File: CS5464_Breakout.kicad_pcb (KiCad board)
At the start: 2 copper layers, 35.6 x 27.9 mm, 25 parts, among them J1 Conn_01x10, U1 CS5464-ISZ, Y1 Crystal

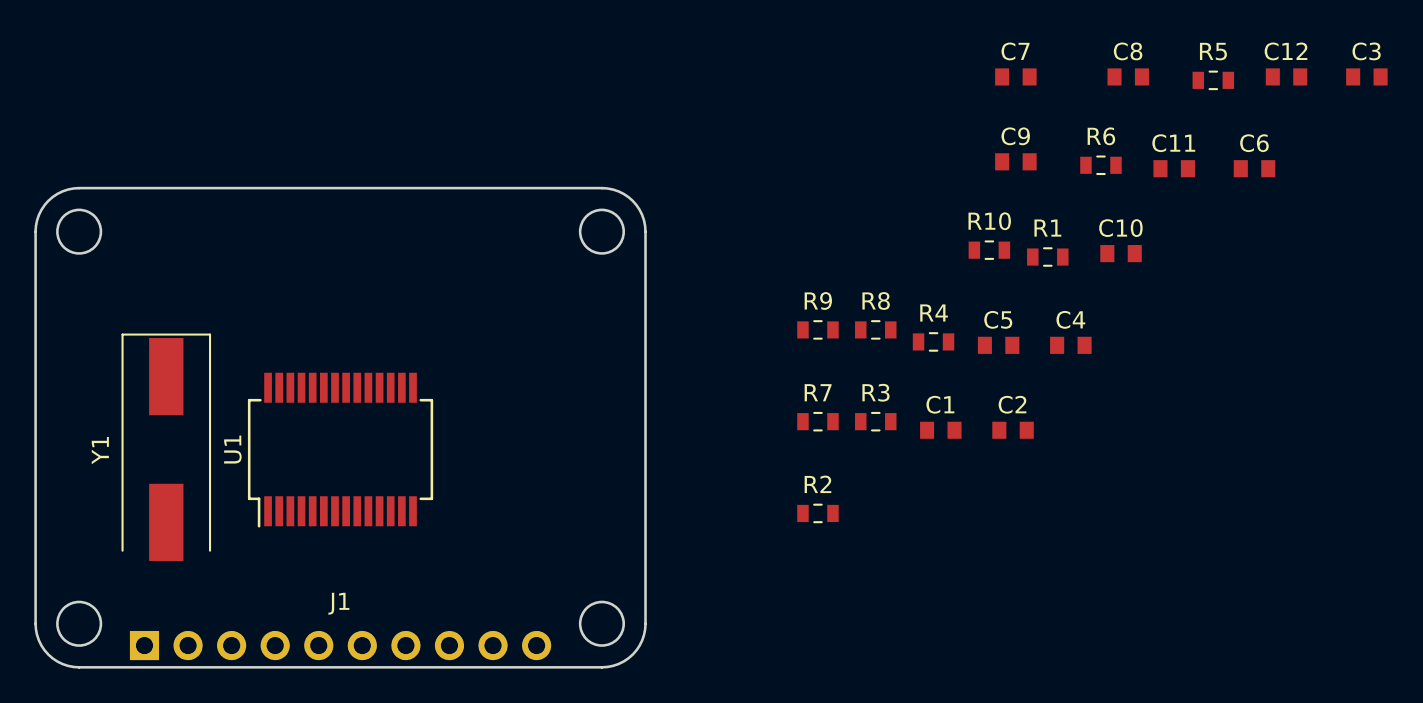
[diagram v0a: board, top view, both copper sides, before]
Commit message: Add logos and part placement
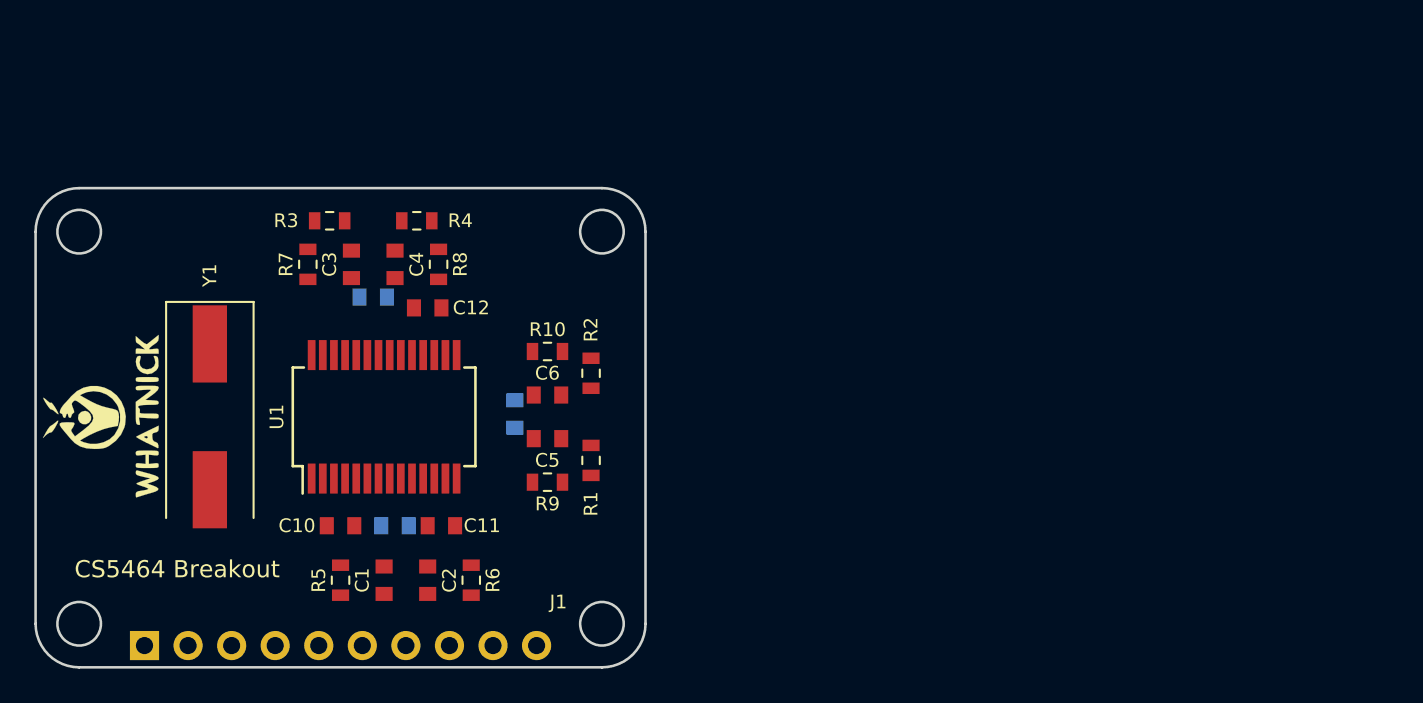
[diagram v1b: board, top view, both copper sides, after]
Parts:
- added G1: LOGO, Whatnick_logo:Whatnick_logo, F.Cu at (114.3, 93.3)
- added LOGO1: Logo_Open_Hardware_Small, Symbol:OSHW-Logo2_7.3x6mm_SilkScreen, B.Cu at (128.9, 94.0)
- C7, C8, C9: moved to B.Cu
- R1, R2, R3, R4: value 1K -> 2.4R
- moved C3 60.2 mm to (128.9, 84.5), turned to 90 degrees
- moved R5 58.6 mm to (128.3, 102.9), turned to 270 degrees
- moved C12 51.9 mm to (133.3, 87.0)
- moved C10 48.2 mm to (128.3, 99.7)
- moved C11 47.5 mm to (134.2, 99.7), turned to 180 degrees
- moved C8 45.9 mm to (130.2, 86.4)
- moved C7 44.7 mm to (131.4, 99.7)
- moved R6 44.0 mm to (135.9, 102.9), turned to 270 degrees
- moved C6 43.3 mm to (140.3, 92.1), turned to 180 degrees
- moved C4 39.7 mm to (131.4, 84.5), turned to 270 degrees
- moved C2 35.2 mm to (133.3, 102.9), turned to 90 degrees
- moved R3 33.9 mm to (127.6, 81.9), turned to 180 degrees
- moved C1 33.6 mm to (130.8, 102.9), turned to 270 degrees
- moved C9 32.7 mm to (138.4, 93.2), turned to 90 degrees
- moved R7 31.1 mm to (126.4, 84.5), turned to 90 degrees
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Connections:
- net Net-(U1-Pad23) renamed ~RESET
- net Net-(U1-Pad27) renamed MOSI
- net Net-(U1-Pad5) renamed SCLK
- net Net-(U1-Pad6) renamed MISO
- net Net-(U1-Pad7) renamed ~CS
- C10 pad 2: Net-(C10-Pad2) -> GND
- C11 pad 1: Net-(C11-Pad1) -> GND
- C11 pad 2: Net-(C11-Pad2) -> VREF
- C12 pad 1: Net-(C12-Pad1) -> Net-(C10-Pad1)
- C12 pad 2: Net-(C12-Pad2) -> GND
- C3 pad 1: IIN+ -> IIN1+
- C4 pad 2: IIN- -> IIN1-
- C8 pad 1: IIN+ -> IIN1+
- C8 pad 2: IIN- -> IIN1-
- R7 pad 1: IIN+ -> IIN1+
- R8 pad 1: IIN- -> IIN1-
- U1 pad 10: Net-(U1-Pad10) -> VIN-
- U1 pad 11: Net-(U1-Pad11) -> VREF
- U1 pad 12: Net-(U1-Pad12) -> VREF
- U1 pad 15: Net-(U1-Pad15) -> IIN2-
- U1 pad 16: Net-(U1-Pad16) -> IIN2+
- U1 pad 18: Net-(U1-Pad18) -> Net-(C10-Pad1)
- U1 pad 19: Net-(U1-Pad19) -> IIN1-
- U1 pad 20: Net-(U1-Pad20) -> IIN1+
- U1 pad 3: Net-(U1-Pad3) -> Net-(C10-Pad1)
- U1 pad 9: Net-(U1-Pad9) -> VIN+
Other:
- board text added: "CS5464 Breakout"

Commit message: Update schematic and PCB
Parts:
- added CPUCLK1: CPUCLK, TestPoint:TestPoint_Pad_1.5x1.5mm, B.Cu at (119.4, 96.5)
- added MODE1: MODE, TestPoint:TestPoint_Pad_1.5x1.5mm, B.Cu at (122.6, 96.5)
- added PFMON1: PFMON, TestPoint:TestPoint_Pad_1.5x1.5mm, B.Cu at (122.6, 90.2)
- added ~E1: ~E1, TestPoint:TestPoint_Pad_1.5x1.5mm, B.Cu at (116.2, 96.5)
- added ~E2: ~E2, TestPoint:TestPoint_Pad_1.5x1.5mm, B.Cu at (113.0, 96.5)
- added ~E3: ~E3, TestPoint:TestPoint_Pad_1.5x1.5mm, B.Cu at (119.4, 90.2)
- added ~INT1: ~INT, TestPoint:TestPoint_Pad_1.5x1.5mm, B.Cu at (113.0, 90.2)
- added ~RESET1: ~RESET, TestPoint:TestPoint_Pad_1.5x1.5mm, B.Cu at (116.2, 90.2)
- moved LOGO1 5.75 mm to (134.6, 93.3), turned to 270 degrees
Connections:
- net Net-(J1-Pad5) renamed CS
- C10 pad 1: Net-(C10-Pad1) -> +3V3
- C12 pad 1: Net-(C10-Pad1) -> +3V3
- J1 pad 1: Net-(J1-Pad1) -> +3V3
- J1 pad 10: Net-(J1-Pad10) -> GND
- J1 pad 2: Net-(J1-Pad2) -> VP
- J1 pad 3: Net-(J1-Pad3) -> VN
- J1 pad 4: Net-(J1-Pad4) -> SCLK
- J1 pad 6: Net-(J1-Pad6) -> MISO
- J1 pad 7: Net-(J1-Pad7) -> MOSI
- J1 pad 8: Net-(J1-Pad8) -> IP
- J1 pad 9: Net-(J1-Pad9) -> IN
- U1 pad 18: Net-(C10-Pad1) -> +3V3
- U1 pad 23: ~RESET -> Net-(U1-Pad23)
- U1 pad 3: Net-(C10-Pad1) -> +3V3

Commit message: Complete place and route and generate Gerbers
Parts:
- added IN2: IN2, TestPoint:TestPoint_Pad_1.5x1.5mm, B.Cu at (143.4, 91.5)
- added IP2: IP2, TestPoint:TestPoint_Pad_1.5x1.5mm, B.Cu at (143.4, 94.5)
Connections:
- J1 pad 5: CS -> ~CS
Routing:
- net GND: track 0.00 -> 70.4 mm, vias 0 -> 13
- net IP: track 0.00 -> 29.8 mm, vias 0 -> 1
- net +3V3: track 0.00 -> 29.7 mm
- net IN: track 0.00 -> 26.9 mm, vias 0 -> 1
- net Net-(U1-Pad26): track 0.00 -> 19.8 mm, vias 0 -> 1
- net MOSI: track 0.00 -> 19.3 mm, vias 0 -> 1
- net Net-(U1-Pad24): track 0.00 -> 18.9 mm, vias 0 -> 1
- net Net-(U1-Pad23): track 0.00 -> 18.2 mm, vias 0 -> 1
- net Net-(U1-Pad25): track 0.00 -> 16.7 mm, vias 0 -> 1
- net VN: track 0.00 -> 16.6 mm
- net SCLK: track 0.00 -> 14.9 mm, vias 0 -> 1
- net Net-(U1-Pad22): track 0.00 -> 14.7 mm, vias 0 -> 1
- net IIN2+: track 0.00 -> 11.8 mm, vias 0 -> 1
- net Net-(PFMON1-Pad1): track 0.00 -> 11.8 mm, vias 0 -> 1
- net VIN+: track 0.00 -> 11.6 mm, vias 0 -> 1
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- added copper zone on B.Cu, net GND
- added copper zone on F.Cu, net GND
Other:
- board text added: "by Tisham Dhar http://whatnick.com v0.1 06/02/2019"

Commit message: Add part numbers
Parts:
- Y1: value Crystal -> 4.096MHz
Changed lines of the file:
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@@
       (effects (font (size 0.8 0.8) (thickness 0.2)))
     )
-    (fp_text value Crystal (at 0 3.55 270) (layer F.Fab)
+    (fp_text value 4.096MHz (at 0 3.55 270) (layer F.Fab)
       (effects (font (size 1 1) (thickness 0.15)))
     )
